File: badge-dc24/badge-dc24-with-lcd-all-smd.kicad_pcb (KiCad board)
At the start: 2 copper layers, 30 parts, among them U1 ESP-12E, U2 TSOP38238, U3 74HC595, U4 MC78L05ACH

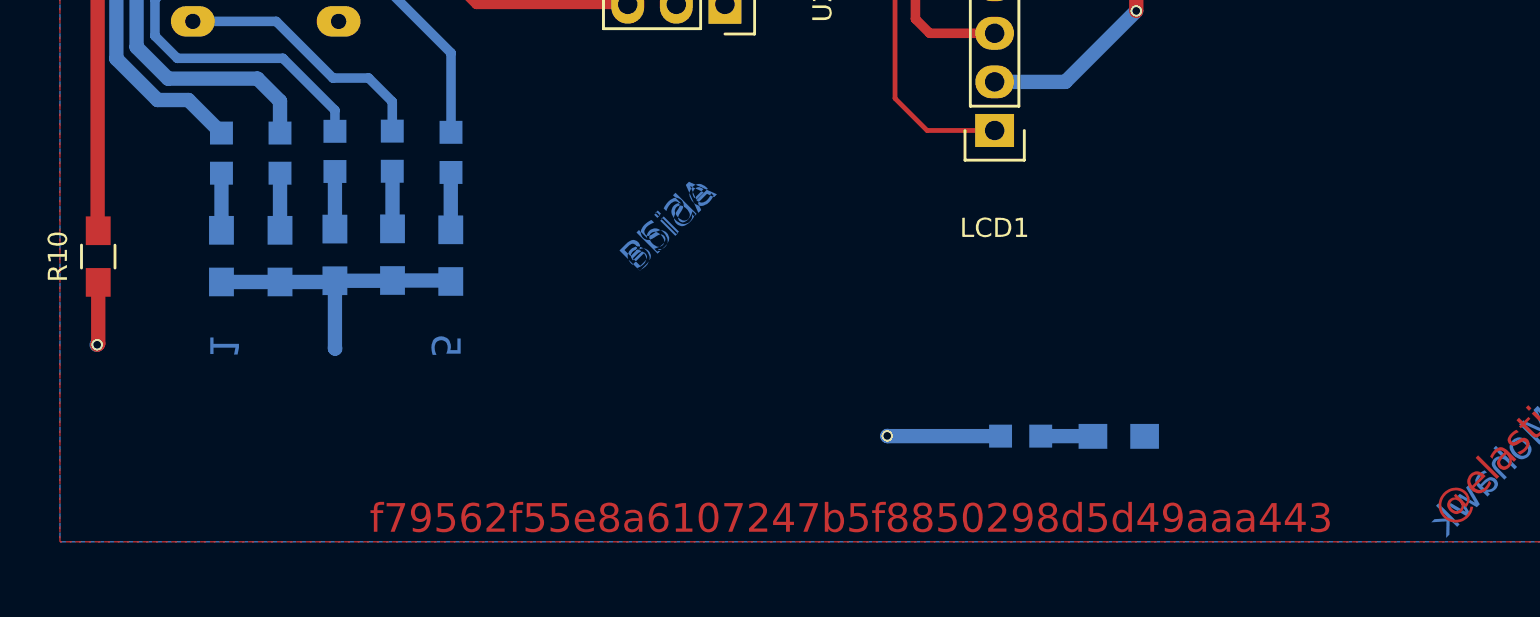
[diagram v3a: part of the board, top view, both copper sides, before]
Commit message: Thicker tracks
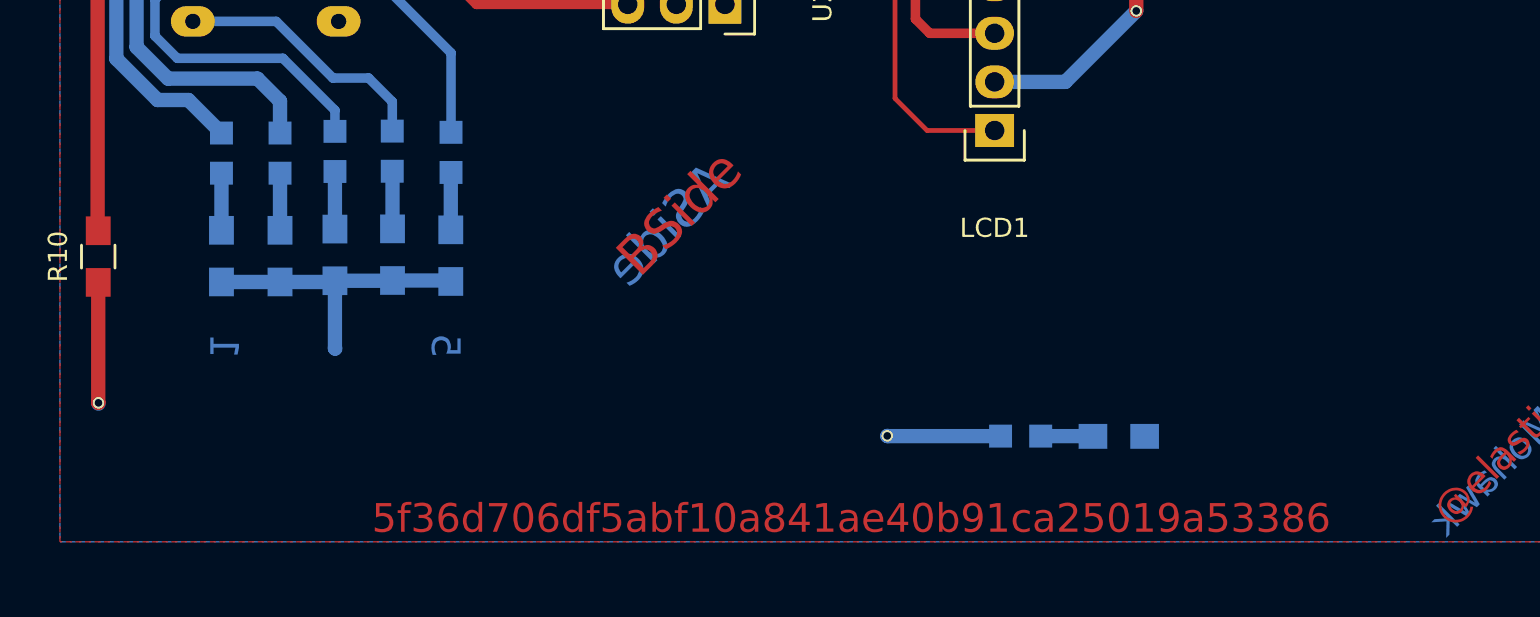
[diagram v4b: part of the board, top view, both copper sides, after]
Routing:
- net GND: track 72.4 -> 75.5 mm
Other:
- board text added: "5f36d706df5abf10a841ae40b91ca25019a53386"
- board text removed: "f79562f55e8a6107247b5f8850298d5d49aaa443"
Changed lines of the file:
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@@
     (links 69)
     (no_connects 0)
-    (area 0 0 0 0)
+    (area 49.57 58.46 152.36 130.77)
     (thickness 1.6)
     (drawings 13)
@@
       (net 23 "Net-(RESET1-Pad2)"))
   )
-  (gr_text BSide (at 86.54796 108.1278 45) (layer B.Cu)
-    (effects (font (size 1.5 1.5) (thickness 0.3)))
+  (gr_text BSide (at 87.18804 107.53344 45) (layer F.Cu)
+    (effects (font (size 2 2) (thickness 0.3)))
   )
   (gr_text ASide (at 86.59368 108.11764 45) (layer B.Cu)
-    (effects (font (size 1.5 1.5) (thickness 0.3)) (justify mirror))
+    (effects (font (size 2 2) (thickness 0.3)) (justify mirror))
   )
   (gr_text 5 (at 74.94016 114.44732 270) (layer B.Cu)
@@
     (effects (font (size 1.5 1.5) (thickness 0.3)))
   )
-  (gr_text f79562f55e8a6107247b5f8850298d5d49aaa443 (at 96.1644 123.4948) (layer F.Cu)
+  (gr_text 5f36d706df5abf10a841ae40b91ca25019a53386 (at 96.1644 123.4948) (layer F.Cu)
     (effects (font (size 1.5 1.5) (thickness 0.3)))
   )
@@
   (segment (start 75.25002 82.2503) (end 75.7174 82.2503) (width 0.5) (layer F.Cu) (net 5))
   (segment (start 74.7725 82.2503) (end 75.7174 82.2503) (width 0.5) (layer F.Cu) (net 5) (status 30))
-  (segment (start 61.7474 92.4306) (end 60.74156 92.4306) (width 0.75) (layer B.Cu) (net 6) (status C00000))
-  (segment (start 60.74156 92.4306) (end 58.80608 94.36608) (width 0.75) (layer B.Cu) (net 6) (status 400000))
+  (segment (start 61.7474 92.4306) (end 60.74156 92.4306) (width 0.75) (layer B.Cu) (net 6))
+  (segment (start 60.74156 92.4306) (end 58.80608 94.36608) (width 0.75) (layer B.Cu) (net 6))
   (segment (start 58.80608 94.36608) (end 58.80608 98.8568) (width 0.75) (layer B.Cu) (net 6))
   (segment (start 58.80608 98.8568) (end 60.452 100.50272) (width 0.75) (layer B.Cu) (net 6))
   (segment (start 60.452 100.50272) (end 65.1256 100.50272) (width 0.75) (layer B.Cu) (net 6))
   (segment (start 65.1256 100.50272) (end 66.30416 101.68128) (width 0.75) (layer B.Cu) (net 6))
-  (segment (start 66.30416 101.68128) (end 66.30416 103.34752) (width 0.75) (layer B.Cu) (net 6) (status 800000))
-  (segment (start 61.7474 89.8906) (end 60.94476 89.8906) (width 0.75) (layer B.Cu) (net 8) (status C00000))
-  (segment (start 60.94476 89.8906) (end 57.74944 93.08592) (width 0.75) (layer B.Cu) (net 8) (status 400000))
+  (segment (start 66.30416 101.68128) (end 66.30416 103.34752) (width 0.75) (layer B.Cu) (net 6))
+  (segment (start 61.7474 89.8906) (end 60.94476 89.8906) (width 0.75) (layer B.Cu) (net 8))
+  (segment (start 60.94476 89.8906) (end 57.74944 93.08592) (width 0.75) (layer B.Cu) (net 8))
   (segment (start 57.74944 93.08592) (end 57.74944 99.4664) (width 0.75) (layer B.Cu) (net 8))
   (segment (start 57.74944 99.4664) (end 59.90336 101.62032) (width 0.75) (layer B.Cu) (net 8))
   (segment (start 59.90336 101.62032) (end 61.51626 101.62032) (width 0.75) (layer B.Cu) (net 8))
-  (segment (start 61.51626 101.62032) (end 63.24346 103.34752) (width 0.75) (layer B.Cu) (net 8) (status 800000))
+  (segment (start 61.51626 101.62032) (end 63.24346 103.34752) (width 0.75) (layer B.Cu) (net 8))
   (segment (start 69.3674 87.3506) (end 69.3674 87.0966) (width 0.5) (layer F.Cu) (net 9))
   (segment (start 69.3674 87.0966) (end 72.644 83.82) (width 0.5) (layer F.Cu) (net 9))
@@
   (segment (start 69.3674 87.3506) (end 69.3674 86.8426) (width 0.25) (layer F.Cu) (net 9))
   (segment (start 75.6021 80.3656) (end 75.7174 80.2503) (width 0.75) (layer F.Cu) (net 9) (status 30))
-  (segment (start 56.769 87.5284) (end 61.5696 87.5284) (width 0.75) (layer F.Cu) (net 10) (status C00000))
-  (segment (start 61.5696 87.5284) (end 61.7474 87.3506) (width 0.75) (layer F.Cu) (net 10) (status C00000))
+  (segment (start 56.769 87.5284) (end 61.5696 87.5284) (width 0.75) (layer F.Cu) (net 10))
+  (segment (start 61.5696 87.5284) (end 61.7474 87.3506) (width 0.75) (layer F.Cu) (net 10))
   (segment (start 69.3674 84.8106) (end 69.94652 84.8106) (width 0.5) (layer F.Cu) (net 11))
   (segment (start 69.94652 84.8106) (end 71.85152 82.9056) (width 0.5) (layer F.Cu) (net 11))
@@
   (segment (start 71.85152 82.9056) (end 71.85152 79.36992) (width 0.5) (layer F.Cu) (net 11))
   (segment (start 69.3674 84.8106) (end 70.0278 84.8106) (width 0.25) (layer F.Cu) (net 11))
-  (segment (start 56.769 84.9884) (end 61.5696 84.9884) (width 0.75) (layer F.Cu) (net 12) (status C00000))
-  (segment (start 61.5696 84.9884) (end 61.7474 84.8106) (width 0.75) (layer F.Cu) (net 12) (status C00000))
-  (segment (start 56.769 82.4484) (end 61.5696 82.4484) (width 0.75) (layer F.Cu) (net 13) (status C00000))
-  (segment (start 61.5696 82.4484) (end 61.7474 82.2706) (width 0.75) (layer F.Cu) (net 13) (status C00000))
-  (segment (start 56.80202 111.1542) (end 56.80202 114.35842) (width 0.75) (layer F.Cu) (net 15) (status 400000))
-  (segment (start 56.74614 114.4143) (end 56.7182 114.4143) (width 0.75) (layer B.Cu) (net 15))
-  (via (at 56.74614 114.4143) (size 0.6) (drill 0.4) (layers F.Cu B.Cu) (net 15))
-  (segment (start 56.80202 114.35842) (end 56.74614 114.4143) (width 0.75) (layer F.Cu) (net 15))
+  (segment (start 56.769 84.9884) (end 61.5696 84.9884) (width 0.75) (layer F.Cu) (net 12))
+  (segment (start 61.5696 84.9884) (end 61.7474 84.8106) (width 0.75) (layer F.Cu) (net 12))
+  (segment (start 56.769 82.4484) (end 61.5696 82.4484) (width 0.75) (layer F.Cu) (net 13))
+  (segment (start 61.5696 82.4484) (end 61.7474 82.2706) (width 0.75) (layer F.Cu) (net 13))
+  (segment (start 56.80202 111.1542) (end 56.80202 117.4369) (width 0.75) (layer F.Cu) (net 15) (status 400000))
+  (segment (start 56.81472 117.4496) (end 56.81472 117.49024) (width 0.75) (layer B.Cu) (net 15))
+  (via (at 56.81472 117.4496) (size 0.6) (drill 0.4) (layers F.Cu B.Cu) (net 15))
+  (segment (start 56.80202 117.4369) (end 56.81472 117.4496) (width 0.75) (layer F.Cu) (net 15))
   (segment (start 69.17436 111.06784) (end 69.17436 114.6048) (width 0.75) (layer B.Cu) (net 15))
   (segment (start 69.17436 114.6048) (end 69.1896 114.62004) (width 0.75) (layer B.Cu) (net 15))
@@
   (segment (start 75.22972 105.42016) (end 75.24242 105.40746) (width 0.75) (layer B.Cu) (net 21) (status 30))
   (segment (start 63.24346 108.43134) (end 63.24346 105.44556) (width 0.75) (layer B.Cu) (net 22) (status 30))
-  (segment (start 57.2114 73.4948) (end 57.2114 74.30052) (width 0.75) (layer F.Cu) (net 23) (status 400000))
-  (segment (start 73.50506 72.2503) (end 75.7174 72.2503) (width 0.75) (layer F.Cu) (net 23) (status 800000))
+  (segment (start 57.2114 73.4948) (end 57.2114 74.30052) (width 0.75) (layer F.Cu) (net 23))
+  (segment (start 73.50506 72.2503) (end 75.7174 72.2503) (width 0.75) (layer F.Cu) (net 23))
   (segment (start 70.22592 75.52944) (end 73.50506 72.2503) (width 0.75) (layer F.Cu) (net 23))
   (segment (start 58.44032 75.52944) (end 70.22592 75.52944) (width 0.75) (layer F.Cu) (net 23))
@@
   (segment (start 103.6574 87.9729) (end 107.7303 87.9729) (width 0.75) (layer F.Cu) (net 36) (status 30))
   (segment (start 107.7303 87.9729) (end 107.8103 87.8929) (width 0.75) (layer F.Cu) (net 36) (status 30))
-  (segment (start 56.769 90.0684) (end 56.769 108.42118) (width 0.75) (layer F.Cu) (net 37) (status C00000))
-  (segment (start 56.769 108.42118) (end 56.80202 108.4542) (width 0.75) (layer F.Cu) (net 37) (status C00000))
+  (segment (start 56.769 90.0684) (end 56.769 108.42118) (width 0.75) (layer F.Cu) (net 37))
+  (segment (start 56.769 108.42118) (end 56.80202 108.4542) (width 0.75) (layer F.Cu) (net 37))
   (segment (start 91.7174 78.2503) (end 89.6945 78.2503) (width 0.25) (layer F.Cu) (net 38) (status 10))
   (segment (start 100.1268 103.2129) (end 103.6574 103.2129) (width 0.25) (layer F.Cu) (net 38) (status 20))

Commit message: Updated git version
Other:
- board text added: "28df4735957a0b982dbc1d2027cbe393688ae2d4"
- board text removed: "5f36d706df5abf10a841ae40b91ca25019a53386"
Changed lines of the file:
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@@
     (effects (font (size 1.5 1.5) (thickness 0.3)))
   )
-  (gr_text 5f36d706df5abf10a841ae40b91ca25019a53386 (at 96.1644 123.4948) (layer F.Cu)
+  (gr_text 28df4735957a0b982dbc1d2027cbe393688ae2d4 (at 96.1644 123.4948) (layer F.Cu)
     (effects (font (size 1.5 1.5) (thickness 0.3)))
   )

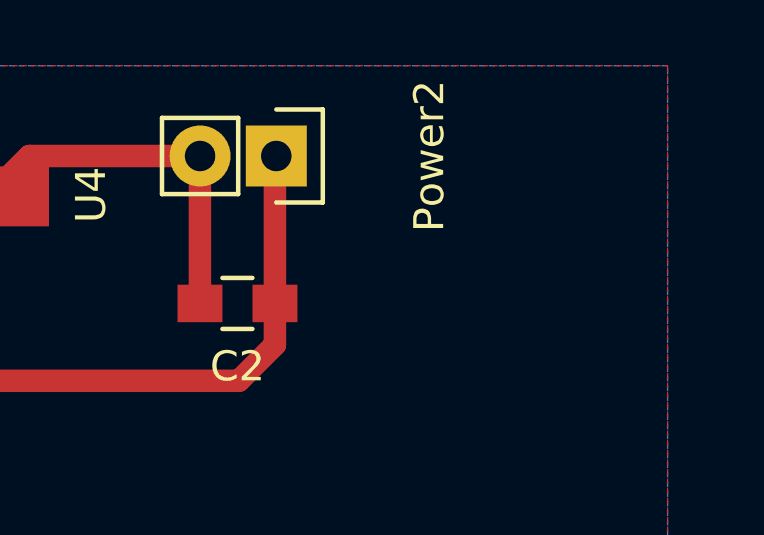
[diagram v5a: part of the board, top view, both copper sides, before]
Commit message: Added USB mini socket
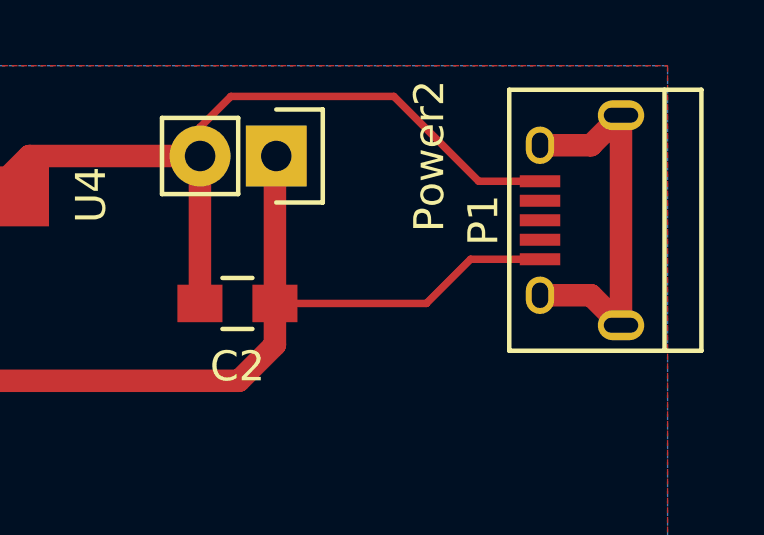
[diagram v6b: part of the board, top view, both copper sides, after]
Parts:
- added P1: USB_OTG, Connect:USB_Micro-B, F.Cu at (144.1, 69.1)
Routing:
- net GND: track 75.5 -> 89.4 mm
- net Net-(P1-Pad6): track 0.00 -> 13.2 mm
- net Net-(C2-Pad1): track 23.6 -> 33.1 mm
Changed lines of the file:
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@@
 (kicad_pcb (version 4) (host pcbnew 4.0.2+e4-6225~38~ubuntu15.10.1-stable)
   (general
-    (links 69)
+    (links 74)
     (no_connects 0)
-    (area 49.57 58.46 152.36 130.77)
+    (area 0 0 0 0)
     (thickness 1.6)
     (drawings 13)
-    (tracks 193)
+    (tracks 206)
     (zones 0)
-    (modules 30)
-    (nets 42)
+    (modules 31)
+    (nets 46)
   )
   (page A4)
@@
   (net 40 "Net-(R9-Pad1)")
   (net 41 "Net-(C2-Pad1)")
+  (net 42 "Net-(P1-Pad2)")
+  (net 43 "Net-(P1-Pad3)")
+  (net 44 "Net-(P1-Pad4)")
+  (net 45 "Net-(P1-Pad6)")
   (net_class Default "This is the default net class."
     (clearance 0.2)
@@
     (add_net "Net-(LCD1-Pad5)")
     (add_net "Net-(LCD1-Pad7)")
+    (add_net "Net-(P1-Pad2)")
+    (add_net "Net-(P1-Pad3)")
+    (add_net "Net-(P1-Pad4)")
+    (add_net "Net-(P1-Pad6)")
     (add_net "Net-(Power1-Pad2)")
     (add_net "Net-(R9-Pad1)")
@@
     (pad 2 smd rect (at 3.975 2.25 270) (size 1.55 1.3) (layers F.Cu F.Paste F.Mask)
       (net 23 "Net-(RESET1-Pad2)"))
+  )
+  (module Connect:USB_Micro-B (layer F.Cu)
+    (at 144.05864 69.09562 90)
+    (descr "Micro USB Type B Receptacle")
+    (tags "USB USB_B USB_micro USB_OTG")
+    (attr smd)
+    (fp_text reference P1 (at 0 -3.45 90) (layer F.SilkS)
+      (effects (font (size 1 1) (thickness 0.15)))
+    )
+    (fp_text value USB_OTG (at 0 4.8 90) (layer F.Fab)
+      (effects (font (size 1 1) (thickness 0.15)))
+    )
+    (fp_line (start -4.6 -2.8) (end 4.6 -2.8) (layer F.CrtYd) (width 0.05))
+    (fp_line (start 4.6 -2.8) (end 4.6 4.05) (layer F.CrtYd) (width 0.05))
+    (fp_line (start 4.6 4.05) (end -4.6 4.05) (layer F.CrtYd) (width 0.05))
+    (fp_line (start -4.6 4.05) (end -4.6 -2.8) (layer F.CrtYd) (width 0.05))
+    (fp_line (start -4.3509 3.81746) (end 4.3491 3.81746) (layer F.SilkS) (width 0.15))
+    (fp_line (start -4.3509 -2.58754) (end 4.3491 -2.58754) (layer F.SilkS) (width 0.15))
+    (fp_line (start 4.3491 -2.58754) (end 4.3491 3.81746) (layer F.SilkS) (width 0.15))
+    (fp_line (start 4.3491 2.58746) (end -4.3509 2.58746) (layer F.SilkS) (width 0.15))
+    (fp_line (start -4.3509 3.81746) (end -4.3509 -2.58754) (layer F.SilkS) (width 0.15))
+    (pad 1 smd rect (at -1.3009 -1.56254 180) (size 1.35 0.4) (layers F.Cu F.Paste F.Mask)
+      (net 41 "Net-(C2-Pad1)"))
+    (pad 2 smd rect (at -0.6509 -1.56254 180) (size 1.35 0.4) (layers F.Cu F.Paste F.Mask)
+      (net 42 "Net-(P1-Pad2)"))
+    (pad 3 smd rect (at -0.0009 -1.56254 180) (size 1.35 0.4) (layers F.Cu F.Paste F.Mask)
+      (net 43 "Net-(P1-Pad3)"))
+    (pad 4 smd rect (at 0.6491 -1.56254 180) (size 1.35 0.4) (layers F.Cu F.Paste F.Mask)
+      (net 44 "Net-(P1-Pad4)"))
+    (pad 5 smd rect (at 1.2991 -1.56254 180) (size 1.35 0.4) (layers F.Cu F.Paste F.Mask)
+      (net 15 GND))
+    (pad 6 thru_hole oval (at -2.5009 -1.56254 180) (size 0.95 1.25) (drill oval 0.55 0.85) (layers *.Cu *.Mask F.SilkS)
+      (net 45 "Net-(P1-Pad6)"))
+    (pad 6 thru_hole oval (at 2.4991 -1.56254 180) (size 0.95 1.25) (drill oval 0.55 0.85) (layers *.Cu *.Mask F.SilkS)
+      (net 45 "Net-(P1-Pad6)"))
+    (pad 6 thru_hole oval (at -3.5009 1.13746 180) (size 1.55 1) (drill oval 1.15 0.5) (layers *.Cu *.Mask F.SilkS)
+      (net 45 "Net-(P1-Pad6)"))
+    (pad 6 thru_hole oval (at 3.4991 1.13746 180) (size 1.55 1) (drill oval 1.15 0.5) (layers *.Cu *.Mask F.SilkS)
+      (net 45 "Net-(P1-Pad6)"))
   )
   (gr_text BSide (at 87.18804 107.53344 45) (layer F.Cu)
@@
   (segment (start 56.769 82.4484) (end 61.5696 82.4484) (width 0.75) (layer F.Cu) (net 13))
   (segment (start 61.5696 82.4484) (end 61.7474 82.2706) (width 0.75) (layer F.Cu) (net 13))
-  (segment (start 56.80202 111.1542) (end 56.80202 117.4369) (width 0.75) (layer F.Cu) (net 15) (status 400000))
+  (segment (start 131.1656 66.9544) (end 131.1656 65.99428) (width 0.25) (layer F.Cu) (net 15) (status C00000))
+  (segment (start 131.1656 65.99428) (end 132.19176 64.96812) (width 0.25) (layer F.Cu) (net 15) (status 400000))
+  (segment (start 140.45322 67.79652) (end 142.4961 67.79652) (width 0.25) (layer F.Cu) (net 15) (status 800000))
+  (segment (start 137.62482 64.96812) (end 140.45322 67.79652) (width 0.25) (layer F.Cu) (net 15))
+  (segment (start 132.19176 64.96812) (end 137.62482 64.96812) (width 0.25) (layer F.Cu) (net 15))
+  (segment (start 56.80202 111.1542) (end 56.80202 117.4369) (width 0.75) (layer F.Cu) (net 15))
   (segment (start 56.81472 117.4496) (end 56.81472 117.49024) (width 0.75) (layer B.Cu) (net 15))
   (via (at 56.81472 117.4496) (size 0.6) (drill 0.4) (layers F.Cu B.Cu) (net 15))
@@
   (segment (start 67.02044 80.66024) (end 67.02044 81.65084) (width 0.5) (layer F.Cu) (net 40))
   (segment (start 63.6486 77.2884) (end 67.02044 80.66024) (width 0.5) (layer F.Cu) (net 40))
+  (segment (start 133.6602 71.8693) (end 138.7094 71.8693) (width 0.25) (layer F.Cu) (net 41) (status 400000))
+  (segment (start 140.18218 70.39652) (end 142.4961 70.39652) (width 0.25) (layer F.Cu) (net 41) (status 800000))
+  (segment (start 138.7094 71.8693) (end 140.18218 70.39652) (width 0.25) (layer F.Cu) (net 41))
   (segment (start 120.17756 69.80174) (end 120.17756 72.19696) (width 0.75) (layer F.Cu) (net 41) (status 10))
   (segment (start 133.6602 73.2482) (end 133.6602 71.8693) (width 0.75) (layer F.Cu) (net 41) (status 20))
@@
   (segment (start 133.6602 71.8693) (end 133.6602 66.9998) (width 0.75) (layer F.Cu) (net 41) (status 30))
   (segment (start 133.6602 66.9998) (end 133.7056 66.9544) (width 0.75) (layer F.Cu) (net 41) (status 30))
+  (segment (start 145.1961 65.59652) (end 145.1961 72.59652) (width 0.75) (layer F.Cu) (net 45) (status C00000))
+  (segment (start 142.4961 71.59652) (end 144.1961 71.59652) (width 0.75) (layer F.Cu) (net 45) (status 400000))
+  (segment (start 144.1961 71.59652) (end 145.1961 72.59652) (width 0.75) (layer F.Cu) (net 45) (status 800000))
+  (segment (start 142.4961 66.59652) (end 144.1961 66.59652) (width 0.75) (layer F.Cu) (net 45) (status 400000))
+  (segment (start 144.1961 66.59652) (end 145.1961 65.59652) (width 0.75) (layer F.Cu) (net 45) (status 800000))
   (zone (net 1) (net_name +3V3) (layer F.Cu) (hatch edge 0.508)
     (connect_pads (clearance 0.508))

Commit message: v0.3 update
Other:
- board text added: "4949bd5106ba81babebe5f0a4540db1eed7f4169"
- board text removed: "28df4735957a0b982dbc1d2027cbe393688ae2d4"
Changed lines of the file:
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@@
     (effects (font (size 1.5 1.5) (thickness 0.3)))
   )
-  (gr_text 28df4735957a0b982dbc1d2027cbe393688ae2d4 (at 96.1644 123.4948) (layer F.Cu)
+  (gr_text 4949bd5106ba81babebe5f0a4540db1eed7f4169 (at 96.1644 123.4948) (layer F.Cu)
     (effects (font (size 1.5 1.5) (thickness 0.3)))
   )
